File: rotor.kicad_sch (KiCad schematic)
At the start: 53 parts, among them J1 Power, J10 Analog, J11 Communication, J12 PWM, J13 PWM, J14 Conn_01x16, J15 Conn_01x16, J16 EL_Relay, J17 Conn_01x02, J18 Conn_01x06, J19 Conn_01x02, J2 PWM, J20 LCD 4x16//, J21 Conn_01x04, J22 Push_button_CW, J23 Push_button_CCW, J24 Push_button_UP, J25 Push_button_DwN, J26 AZ_Relay, J27 Conn_01x02, J28 Conn_01x02, J29 Conn_01x02, J3 Analog, J30 Nextion, J31 Conn_01x02, J32 Conn_01x02, J33 LCD 4x16 I2C, J34 Conn_01x02, J35 GPS Neo7M, J36 Conn_01x02, J37 Push_button_DwN, J4 PWM, J5 Analog, J6 Communication, J7 Digital, J8 Analog, J9 Power, U1 uA7805

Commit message: minor fixes, new iBom, RTM version
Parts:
- removed J18: Conn_01x06, Connector_Molex:Molex_KK-254_AE-6410-06A_1x06_P2.54mm_Vertical, symbol Connector_Generic:Conn_01x06
- removed J27, J28, J32: Conn_01x02, Connector_Molex:Molex_KK-254_AE-6410-02A_1x02_P2.54mm_Vertical, symbol Connector_Generic:Conn_01x02
- J37: value Push_button_DwN -> XT30 connector
- RV1: value R_Potentiometer -> 4k7; footprint (none) -> Potentiometer_SMD:Potentiometer_Bourns_TC33X_Vertical
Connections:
- net +5V: now also J20.2 (Pin_2), J33.3 (Pin_3), RV1.1; no longer J33.2 (Pin_2)
- net GND: now also J33.4 (Pin_4), J37.1 (Pin_1); no longer J33.1 (Pin_1), J37.2 (Pin_2)
- net SCL: now also J33.1 (Pin_1); no longer J33.4 (Pin_4)
- net SDA: now also J33.2 (Pin_2); no longer J33.3 (Pin_3)
- net at C1.2, C4.2, C7.1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: now also J37.2 (Pin_2); no longer J37.1 (Pin_1)
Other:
- note added: "Beware : Regulator could be a µA7805 or LM340 1.5 Amp output current, D2Pack package to allow many peripheral options. A 78L05 (DPack package) could also fit if basic config is used"
- note removed: "Conn_02 facultatif"
- moved on the sheet: C1, C4, C5, C6, C7, C8, H1, H2, H3, H4, J37, U1

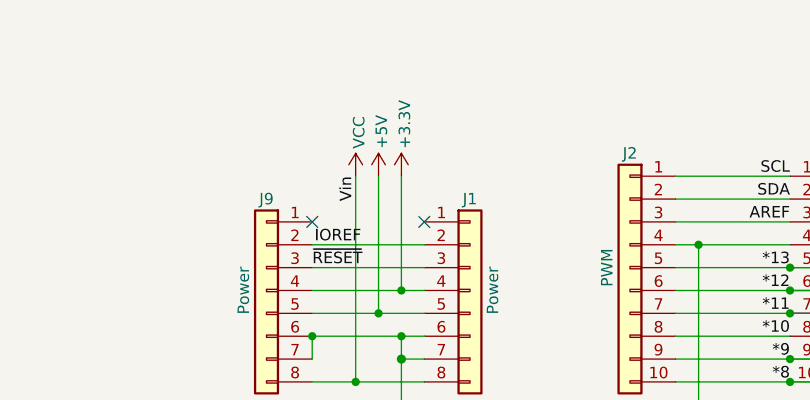
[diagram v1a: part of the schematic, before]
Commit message: updated schematic pdf
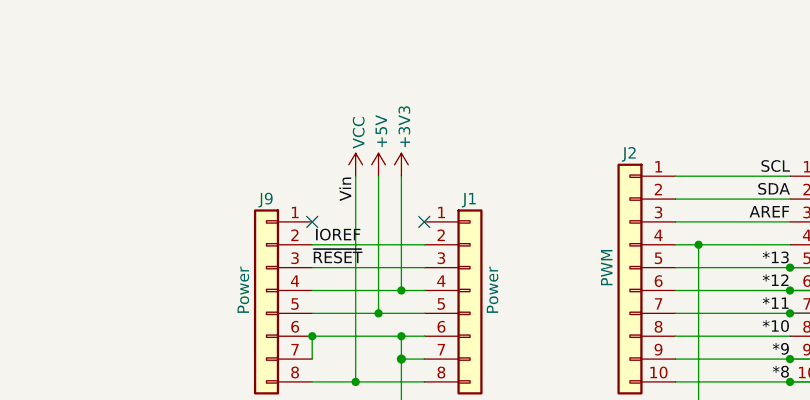
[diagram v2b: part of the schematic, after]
